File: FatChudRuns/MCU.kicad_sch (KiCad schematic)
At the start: 22 parts, among them J2 Z-21320110021001, J3 FTSH-107-01-L-DV-K-P, SW1 SW_Push, SW2 SW_DIP_x01, U1 STM32F107RBT6

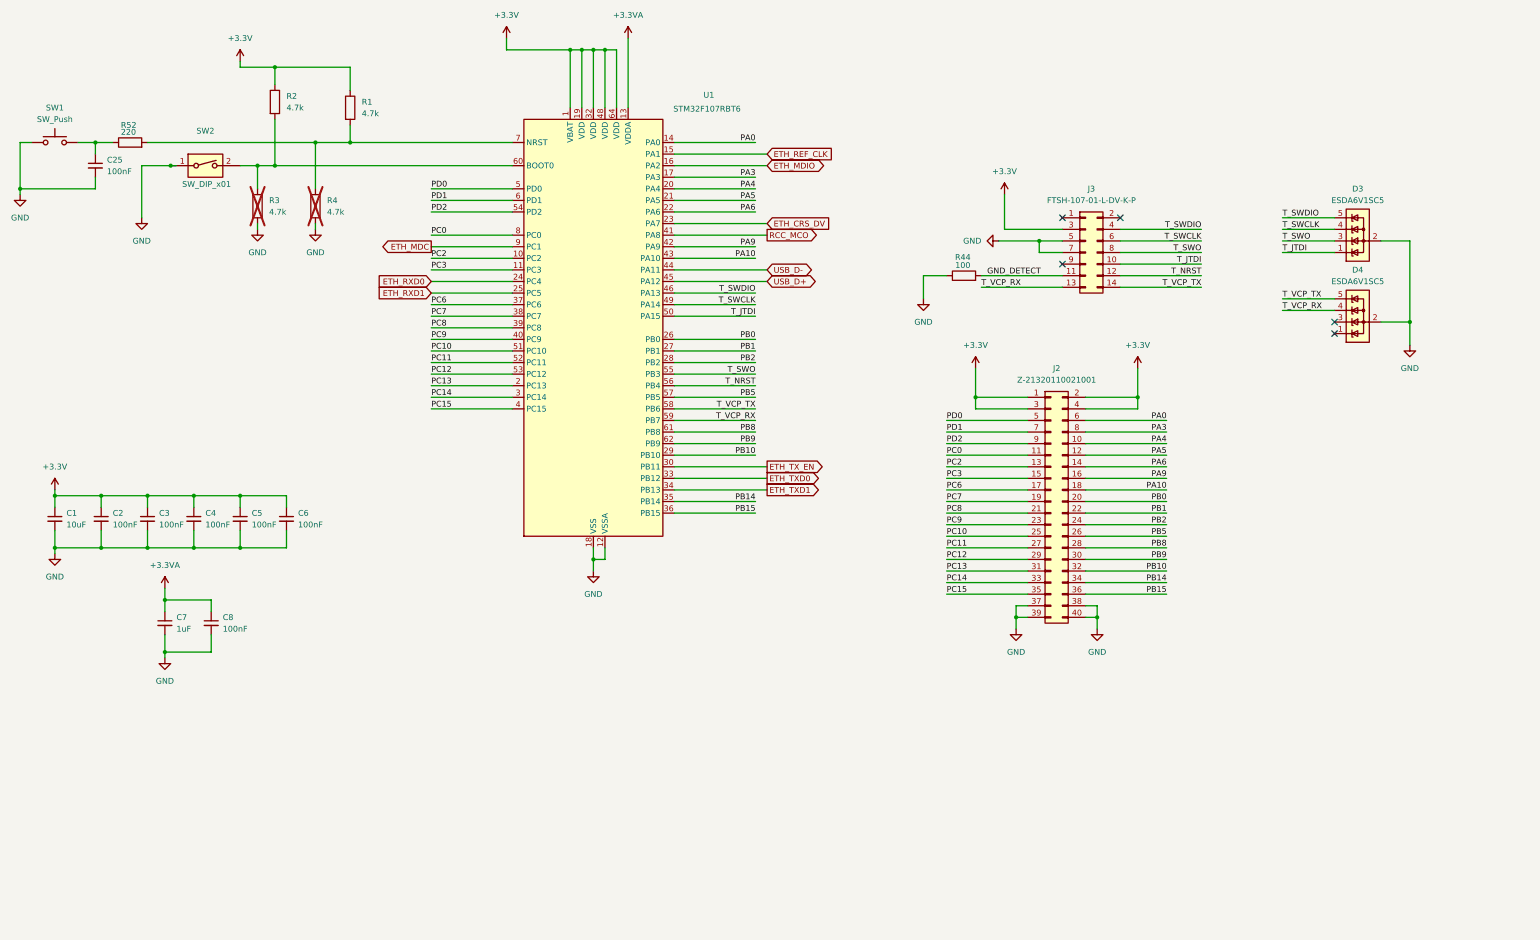
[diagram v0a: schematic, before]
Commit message: added footprint for switches and button - ready for layout
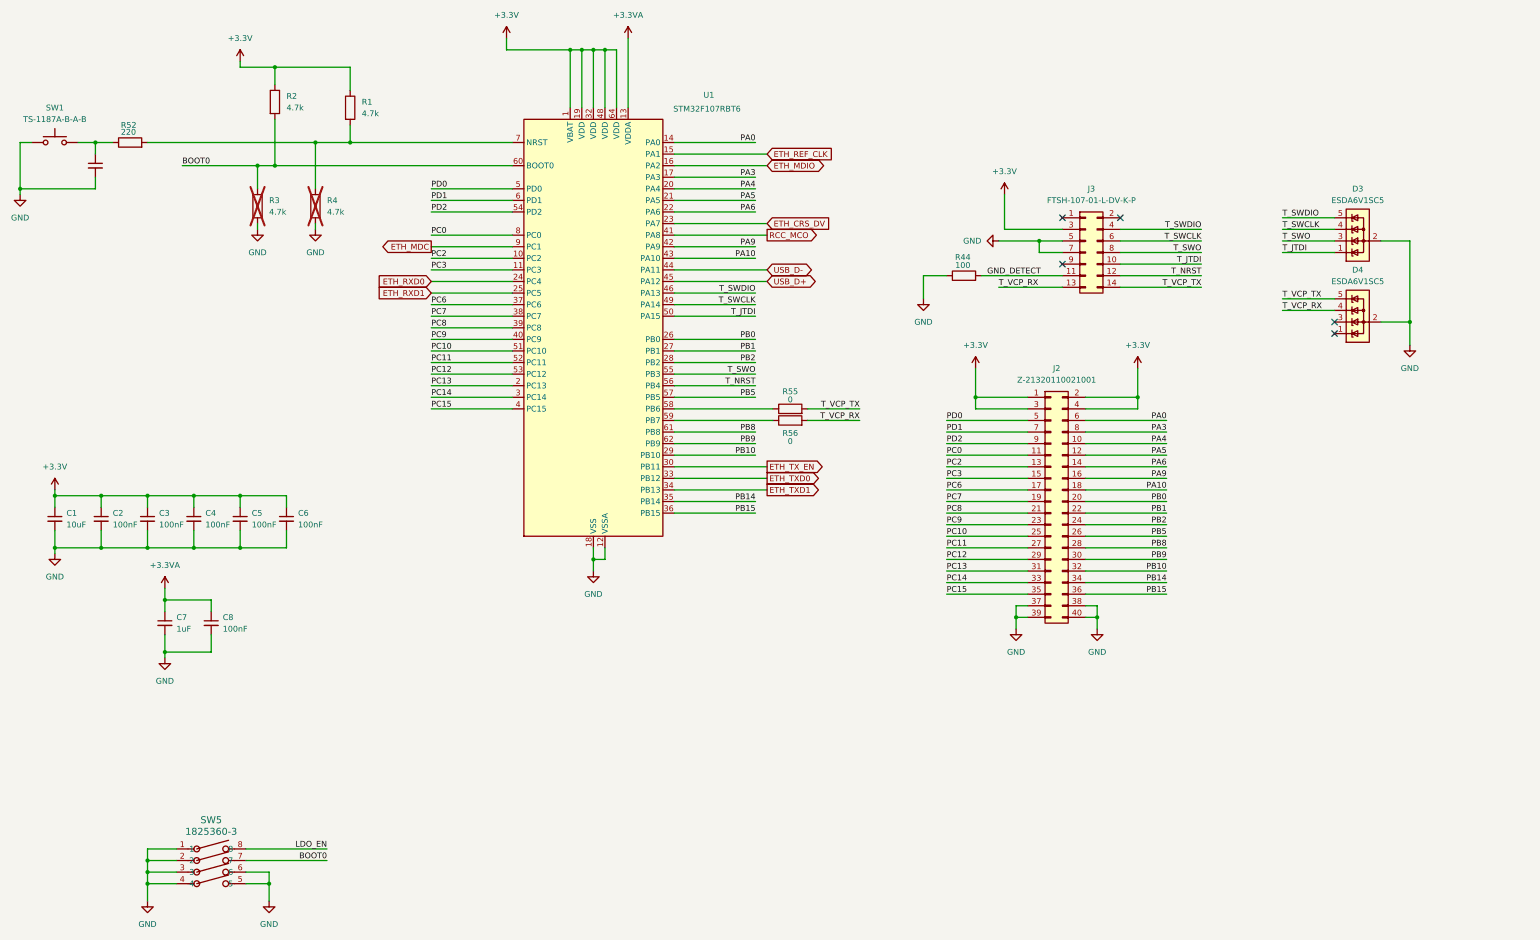
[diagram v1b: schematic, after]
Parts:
- removed SW2: SW_DIP_x01, symbol Switch:SW_DIP_x01
- added R55, R56: 0, Resistor_SMD:R_0603_1608Metric, symbol Device:R
- added SW5: 1825360-3, 1825360_3:SWDIP8_300X185P100, symbol 1825360_3:1825360-3
- SW1: value SW_Push -> TS-1187A-B-A-B; footprint (none) -> Button_Switch_SMD:SW_SPST_TL3342
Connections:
- net GND: now also SW5.1, SW5.2, SW5.3, SW5.4, SW5.5, SW5.6
- net T_VCP_RX: now also R56.2; no longer U1.59 (PB7)
- net T_VCP_TX: now also R55.2; no longer U1.58 (PB6)
- net BOOT0: now reaches R2.2, R3.1, U1.60 (BOOT0)
- net BOOT0: now also SW5.7
- new net: R55.1, U1.58 (PB6)
- new net: R56.1, U1.59 (PB7)
- new net LDO_EN: SW5.8

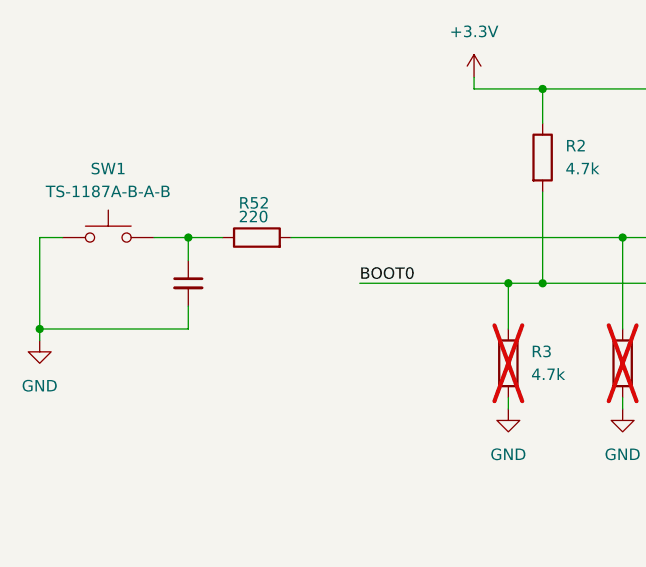
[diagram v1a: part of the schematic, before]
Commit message: setup stackup and constraints
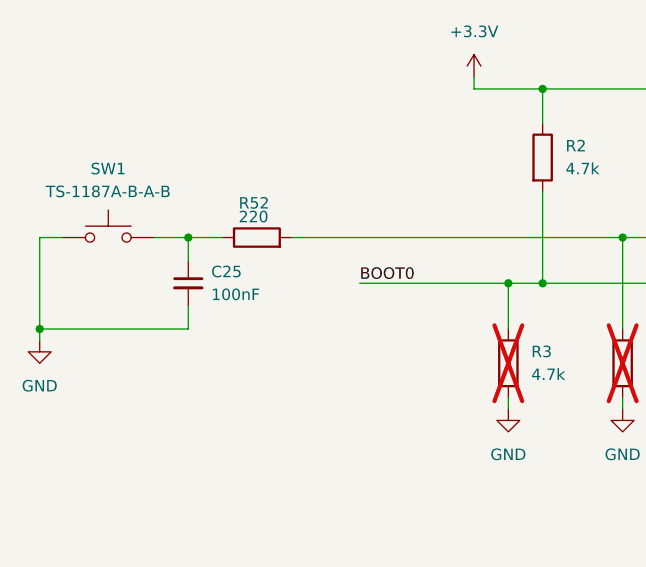
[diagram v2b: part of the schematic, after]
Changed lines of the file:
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@@
 				)
 				(justify left)
-				(hide yes)
 			)
 		)
@@
 				)
 				(justify left)
-				(hide yes)
 			)
 		)

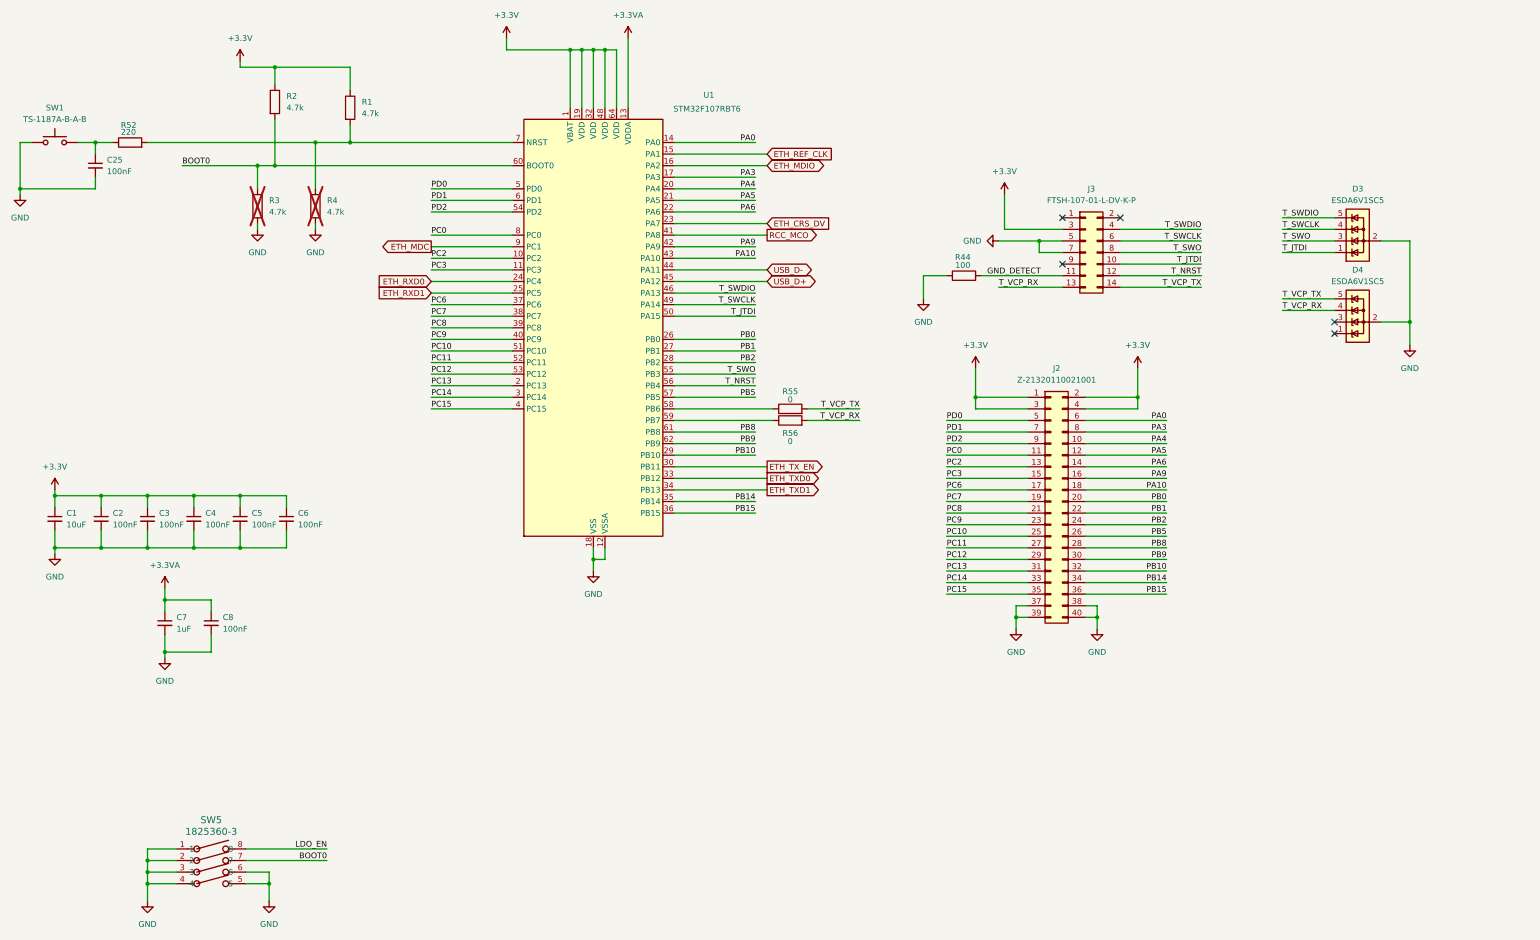
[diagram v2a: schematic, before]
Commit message: added 4pF caps and Rext to XTAL, initial placement of PCB, added board outline and gnd plane
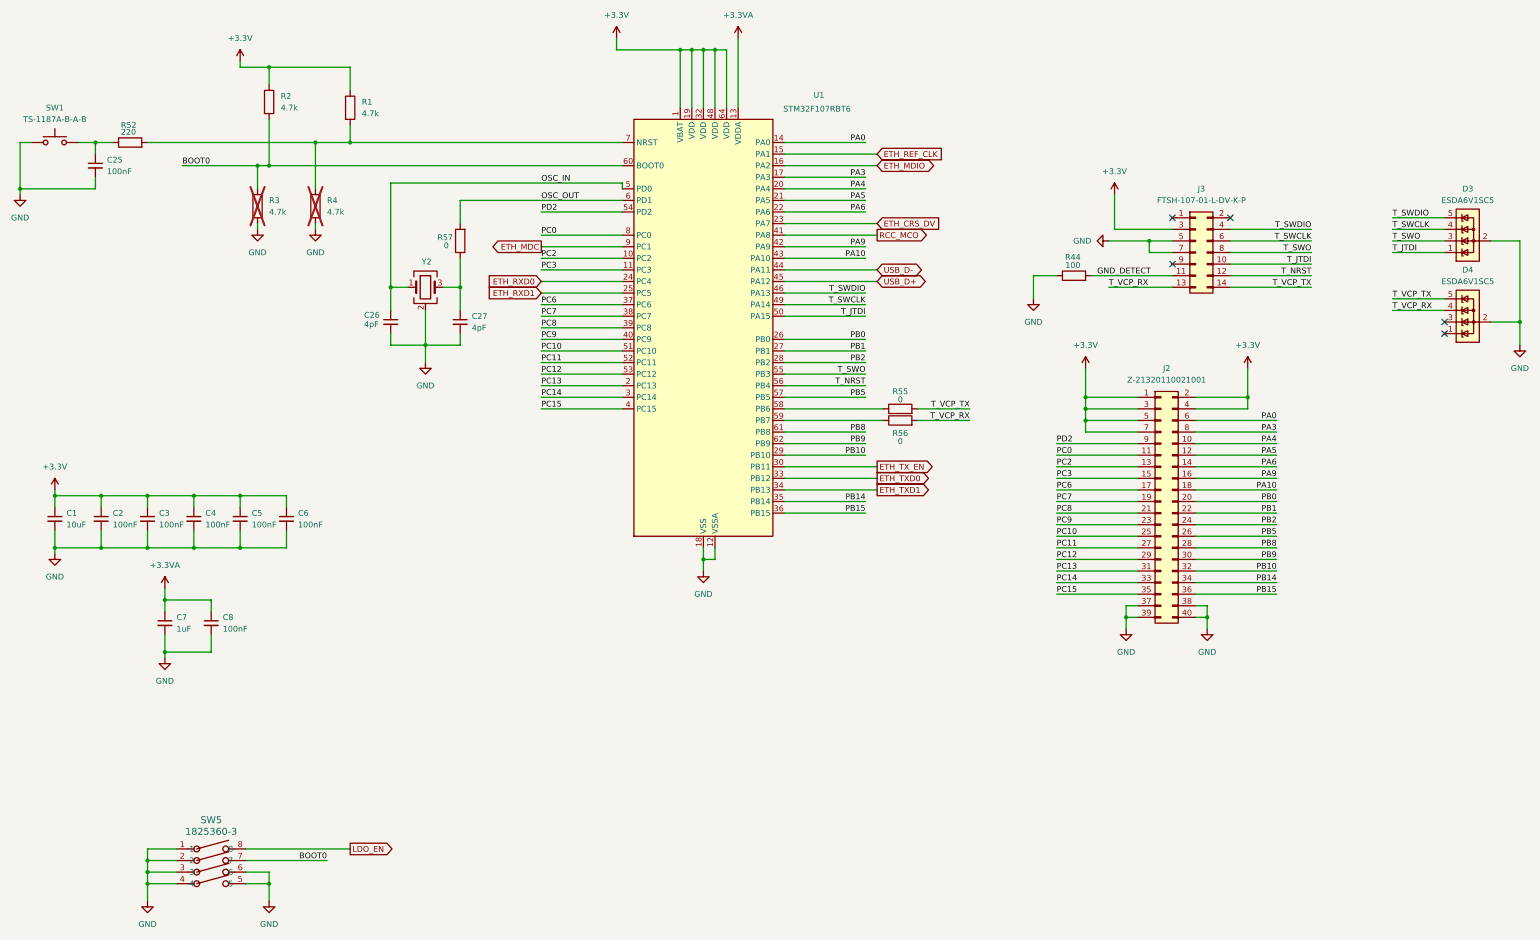
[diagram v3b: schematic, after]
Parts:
- added C26, C27: 4pF, Capacitor_SMD:C_0603_1608Metric, symbol Device:C_Small
- added R57: 0, Resistor_SMD:R_0603_1608Metric, symbol Device:R
- added Y2: ABM8G-25.000MHZ-B4Y-T, Crystal:Crystal_SMD_Abracon_ABM8AIG-4Pin_3.2x2.5mm, symbol Device:Crystal_GND24
- SW5: footprint 1825360_3:SWDIP8_300X185P100 -> SWDIP8_300X185P100
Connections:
- net +3.3V: now also J2.5 (Pin_5), J2.7 (Pin_7)
- net GND: now also C26.2, C27.2, Y2.2 (G), Y2.4 (G)
- net PD0 renamed OSC_IN
- net OSC_IN: now also C26.1, Y2.1; no longer J2.5 (Pin_5)
- net PD1 renamed OSC_OUT
- net OSC_OUT: now also R57.2; no longer J2.7 (Pin_7)
- new net: C27.1, R57.1, Y2.3
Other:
- moved on the sheet: D3, D4, J2, J3, R2, R44, R55, R56, U1

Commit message: routed phy usb and clock
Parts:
- SW5: footprint SWDIP8_300X185P100 -> 1825360_3:SWDIP8_300X185P100

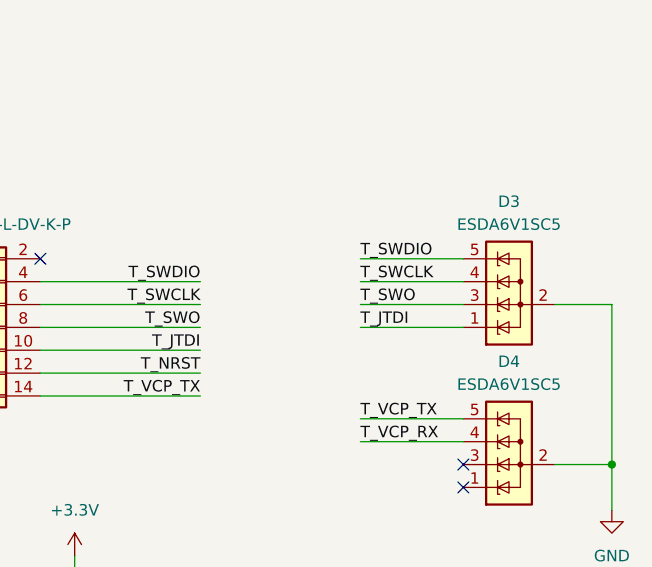
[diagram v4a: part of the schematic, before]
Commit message: routed jtag, ldo, switch, reset button, and decoupling caps. only need GPIO signals
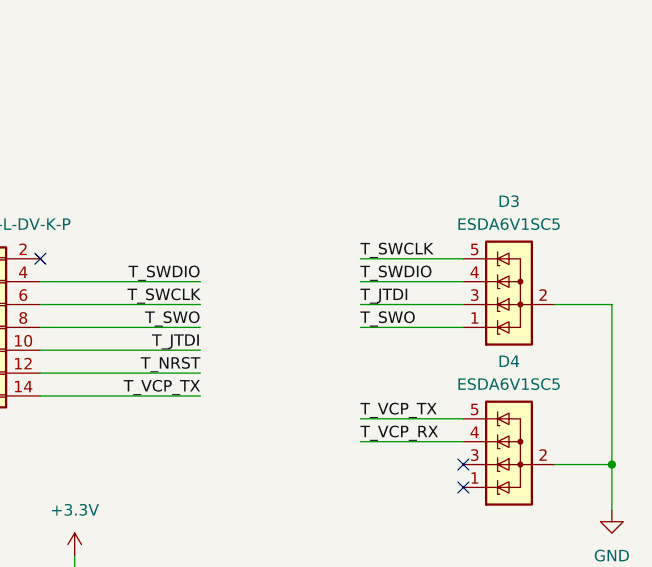
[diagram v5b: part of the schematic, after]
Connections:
- net T_JTDI: now also D3.3 (K); no longer D3.1 (K)
- net T_SWCLK: now also D3.5 (K); no longer D3.4 (K)
- net T_SWDIO: now also D3.4 (K); no longer D3.5 (K)
- net T_SWO: now also D3.1 (K); no longer D3.3 (K)
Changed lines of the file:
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@@
-		)
-	)
-	(label "T_SWDIO"
-		(at 327.66 74.93 0)
-		(effects
-			(font
-				(size 1.27 1.27)
-			)
-			(justify left bottom)
 		)
 	)
@@
 		)
 	)
-	(label "T_SWO"
-		(at 327.66 80.01 0)
-		(effects
-			(font
-				(size 1.27 1.27)
-			)
-			(justify left bottom)
-		)
-	)
 	(label "PA3"
 		(at 212.09 66.04 180)
@@
 		)
 	)
+	(label "T_JTDI"
+		(at 327.66 80.01 0)
+		(effects
+			(font
+				(size 1.27 1.27)
+			)
+			(justify left bottom)
+		)
+	)
 	(label "PA5"
 		(at 302.26 127 180)
@@
 		)
 	)
+	(label "T_SWCLK"
+		(at 327.66 74.93 0)
+		(effects
+			(font
+				(size 1.27 1.27)
+			)
+			(justify left bottom)
+		)
+	)
 	(label "PB8"
 		(at 212.09 121.92 180)
@@
 		)
 	)
-	(label "T_SWCLK"
-		(at 327.66 77.47 0)
-		(effects
-			(font
-				(size 1.27 1.27)
-			)
-			(justify left bottom)
-		)
-	)
 	(label "PC0"
 		(at 140.97 78.74 0)
@@
 		)
 	)
+	(label "T_SWDIO"
+		(at 327.66 77.47 0)
+		(effects
+			(font
+				(size 1.27 1.27)
+			)
+			(justify left bottom)
+		)
+	)
 	(label "PC13"
 		(at 254 152.4 0)
@@
 		)
 	)
+	(label "T_SWO"
+		(at 327.66 82.55 0)
+		(effects
+			(font
+				(size 1.27 1.27)
+			)
+			(justify left bottom)
+		)
+	)
 	(label "PA9"
 		(at 302.26 132.08 180)
@@
 		)
 	)
-	(label "T_JTDI"
-		(at 327.66 82.55 0)
-		(effects
-			(font
-				(size 1.27 1.27)
-			)
-			(justify left bottom)
-		)
-	)
